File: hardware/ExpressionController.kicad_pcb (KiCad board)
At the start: 2 copper layers, 88.6 x 69.8 mm, 129 parts, among them J1 BarrelJack, J2 AudioJack, J3 AudioJack, J4 AudioJack, J5 AudioJack, Q1 DMP3099L-7, U1 ADP7142AUJZ-3.3, U10 74HC595DR, U12 74HC595DR, U14 74AHCT1G125, U15 TMUX1511PWR, U16 TMUX1511PWR, U17 TMUX1511PWR, U18 TMUX1511PWR, U19 TMUX1511PWR, U2 ADP7142AUJZ-5.0, U20 TMUX1511PWR, U21 TMUX1511PWR, U22 TMUX1511PWR, U3 ADP7142AUJZ-2.5, U4 AD7718BRZ, U5 AD7718BRZ, U6 74HC595DR, U8 74HC595DR, Y1 32.768kHz, Y2 32.768kHz

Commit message: added testpoints
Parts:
- added TP1: TestPoint, TestPoint:TestPoint_THTPad_D1.5mm_Drill0.7mm, B.Cu at (128.8, 139.2)
- added TP10: TestPoint, TestPoint:TestPoint_THTPad_D1.5mm_Drill0.7mm, B.Cu at (151.4, 134.4)
- added TP11: TestPoint, TestPoint:TestPoint_THTPad_D1.5mm_Drill0.7mm, B.Cu at (146.3, 134.4)
- added TP12: TestPoint, TestPoint:TestPoint_THTPad_D1.5mm_Drill0.7mm, B.Cu at (199.4, 147.3)
- added TP13: TestPoint, TestPoint:TestPoint_THTPad_D1.5mm_Drill0.7mm, B.Cu at (178.8, 141.0)
- added TP14: TestPoint, TestPoint:TestPoint_THTPad_D1.5mm_Drill0.7mm, B.Cu at (171.2, 140.7)
- added TP15: TestPoint, TestPoint:TestPoint_THTPad_D1.5mm_Drill0.7mm, B.Cu at (186.4, 140.2)
- added TP2: TestPoint, TestPoint:TestPoint_THTPad_D1.5mm_Drill0.7mm, B.Cu at (135.4, 140.5)
- added TP3: TestPoint, TestPoint:TestPoint_THTPad_D1.5mm_Drill0.7mm, B.Cu at (142.0, 141.7)
- added TP4: TestPoint, TestPoint:TestPoint_THTPad_D1.5mm_Drill0.7mm, B.Cu at (122.2, 137.9)
- added TP5: TestPoint, TestPoint:TestPoint_THTPad_D1.5mm_Drill0.7mm, B.Cu at (166.6, 134.4)
- added TP6: TestPoint, TestPoint:TestPoint_THTPad_D1.5mm_Drill0.7mm, B.Cu at (164.1, 134.4)
- added TP7: TestPoint, TestPoint:TestPoint_THTPad_D1.5mm_Drill0.7mm, B.Cu at (159.0, 134.4)
- added TP8: TestPoint, TestPoint:TestPoint_THTPad_D1.5mm_Drill0.7mm, B.Cu at (156.5, 134.4)
- added TP9: TestPoint, TestPoint:TestPoint_THTPad_D1.5mm_Drill0.7mm, B.Cu at (153.9, 134.4)
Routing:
- net GND: track 35.0 -> 44.1 mm, vias 180 -> 179
- net +2.5V: track 106.5 -> 98.8 mm, vias 8 -> 4
- net +3.3VA: track 385.5 -> 378.2 mm, vias 24 -> 20
- net SPI0_NCS2: track 51.2 -> 50.5 mm, vias 1 -> 0
- net +5V: track 235.3 -> 234.6 mm, vias 2 -> 0
- net SR_DATA: track 105.0 -> 105.6 mm
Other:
- board text added: "2.5V"
- board text added: "3.3V"
- board text added: "5V"
- board text added: "CLK"
- board text added: "CS1"
- board text added: "CS2"
- board text added: "DATA"
- board text added: "Expression Adapter Revision 1.0 Amon Benson @ TU Berlin"
- board text added: "LAT"
- board text added: "OE"
- board text added: "RDY1"
- board text added: "RDY2"
- board text added: "RX"
- board text added: "SCLK"
- board text added: "TX"
- board text added: "Vext"

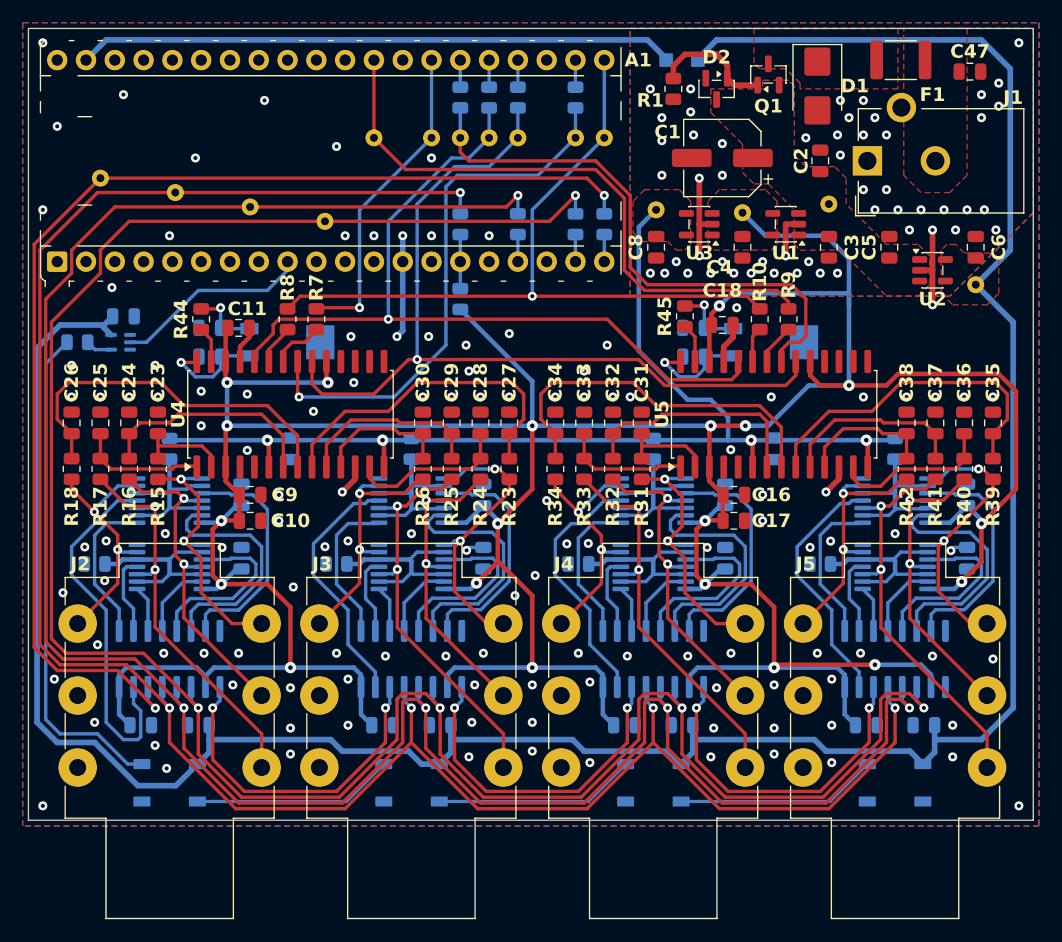
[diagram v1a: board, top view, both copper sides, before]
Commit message: final board, pinouts unchecked
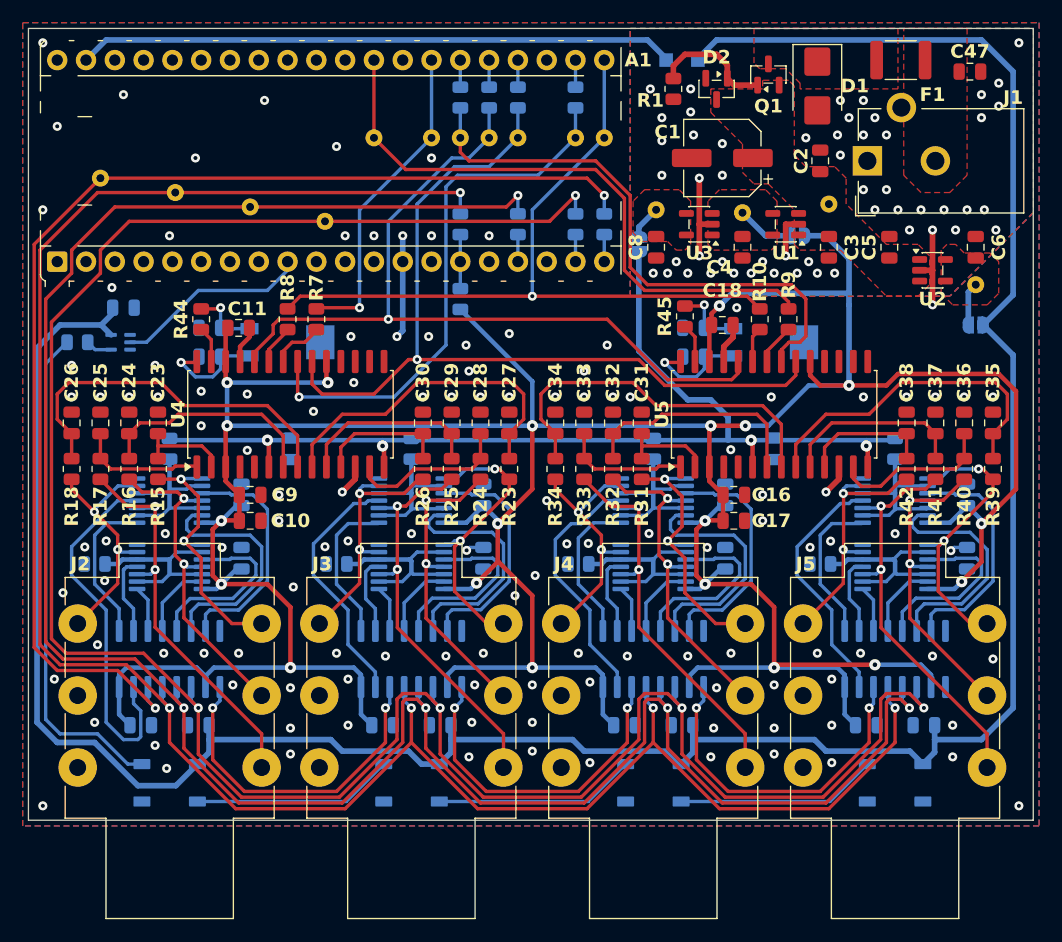
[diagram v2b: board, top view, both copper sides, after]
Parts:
- added JP1: SolderJumper_2_Open, Jumper:SolderJumper-2_P1.3mm_Open_RoundedPad1.0x1.5mm, B.Cu at (183.6, 143.0)
- added JP2: SolderJumper_2_Open, Jumper:SolderJumper-2_P1.3mm_Open_RoundedPad1.0x1.5mm, B.Cu at (169.7, 143.8)
- added JP3: SolderJumper_2_Open, Jumper:SolderJumper-2_P1.3mm_Open_RoundedPad1.0x1.5mm, B.Cu at (199.4, 150.9)
- moved C48 0.76 mm to (124.2, 149.4)
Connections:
- C4 pad 1: +3.3VA -> +3.3VA_RAW
- C6 pad 1: +5V -> +5V_RAW
- C8 pad 1: +2.5V -> +2.5V_RAW
- TP12 pad 1: +5V -> +5V_RAW
- TP13 pad 1: +3.3VA -> +3.3VA_RAW
- TP14 pad 1: +2.5V -> +2.5V_RAW
- U1 pad 4: +3.3VA -> +3.3VA_RAW
- U1 pad 5: +3.3VA -> +3.3VA_RAW
- U2 pad 4: +5V -> +5V_RAW
- U2 pad 5: +5V -> +5V_RAW
- U3 pad 1: +3.3VA -> +3.3VA_RAW
- U3 pad 3: +3.3VA -> +3.3VA_RAW
- U3 pad 4: +2.5V -> +2.5V_RAW
- U3 pad 5: +2.5V -> +2.5V_RAW
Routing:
- net +3.3VA: track 378.2 -> 371.9 mm
- net +3.3VA_RAW: track 0.00 -> 5.02 mm
- net +2.5V: track 98.8 -> 94.5 mm
- net +5V_RAW: track 0.00 -> 3.83 mm
- net +2.5V_RAW: track 0.00 -> 3.03 mm
- added copper zone on F.Cu, net +2.5V_RAW
- added copper zone on F.Cu, net +3.3VA_RAW
- added copper zone on F.Cu, net +5V_RAW
- removed copper zone on F.Cu, net +2.5V
- removed copper zone on F.Cu, net +3.3VA
- removed copper zone on F.Cu, net +5V

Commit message: generated final assembly files
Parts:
- moved C26 0.51 mm to (120.1, 159.5)
- moved R18 0.51 mm to (120.1, 163.6)
- moved C25 0.25 mm to (122.4, 159.5)
- moved R17 0.25 mm to (122.4, 163.6)
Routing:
- net GND: track 44.1 -> 64.3 mm, vias 179 -> 211
- net SR_OE: track 188.8 -> 197.0 mm
- net SR_DATA: track 105.3 -> 112.1 mm
- net SR_LAT: track 200.8 -> 204.4 mm
- net /AnalogFrontend/AnalogQuadChannel1/JACK4: track 22.5 -> 26.1 mm
- net /AnalogFrontend/AnalogQuadChannel1/ADC4: track 32.5 -> 29.6 mm
- net SR_CLK: track 205.6 -> 203.3 mm
- net +5V: track 235.0 -> 235.9 mm
- net Net-(D4-DIN): track 44.2 -> 45.0 mm
- net Net-(U10-QH): track 20.8 -> 21.4 mm
- net Net-(U12-QH): track 20.8 -> 21.4 mm
- net Net-(U16-SEL3): track 20.8 -> 21.4 mm
- net Net-(U15-SEL3): track 20.8 -> 21.4 mm
